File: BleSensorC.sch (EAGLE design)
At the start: 20 parts, among them IC1 PIC16LF18446-I_SS, IC2 SI7020-A20-GM, Q1 SI2333DDS-T1-GE3, T1 VEMT2523SLX01, U1 RN4871-I

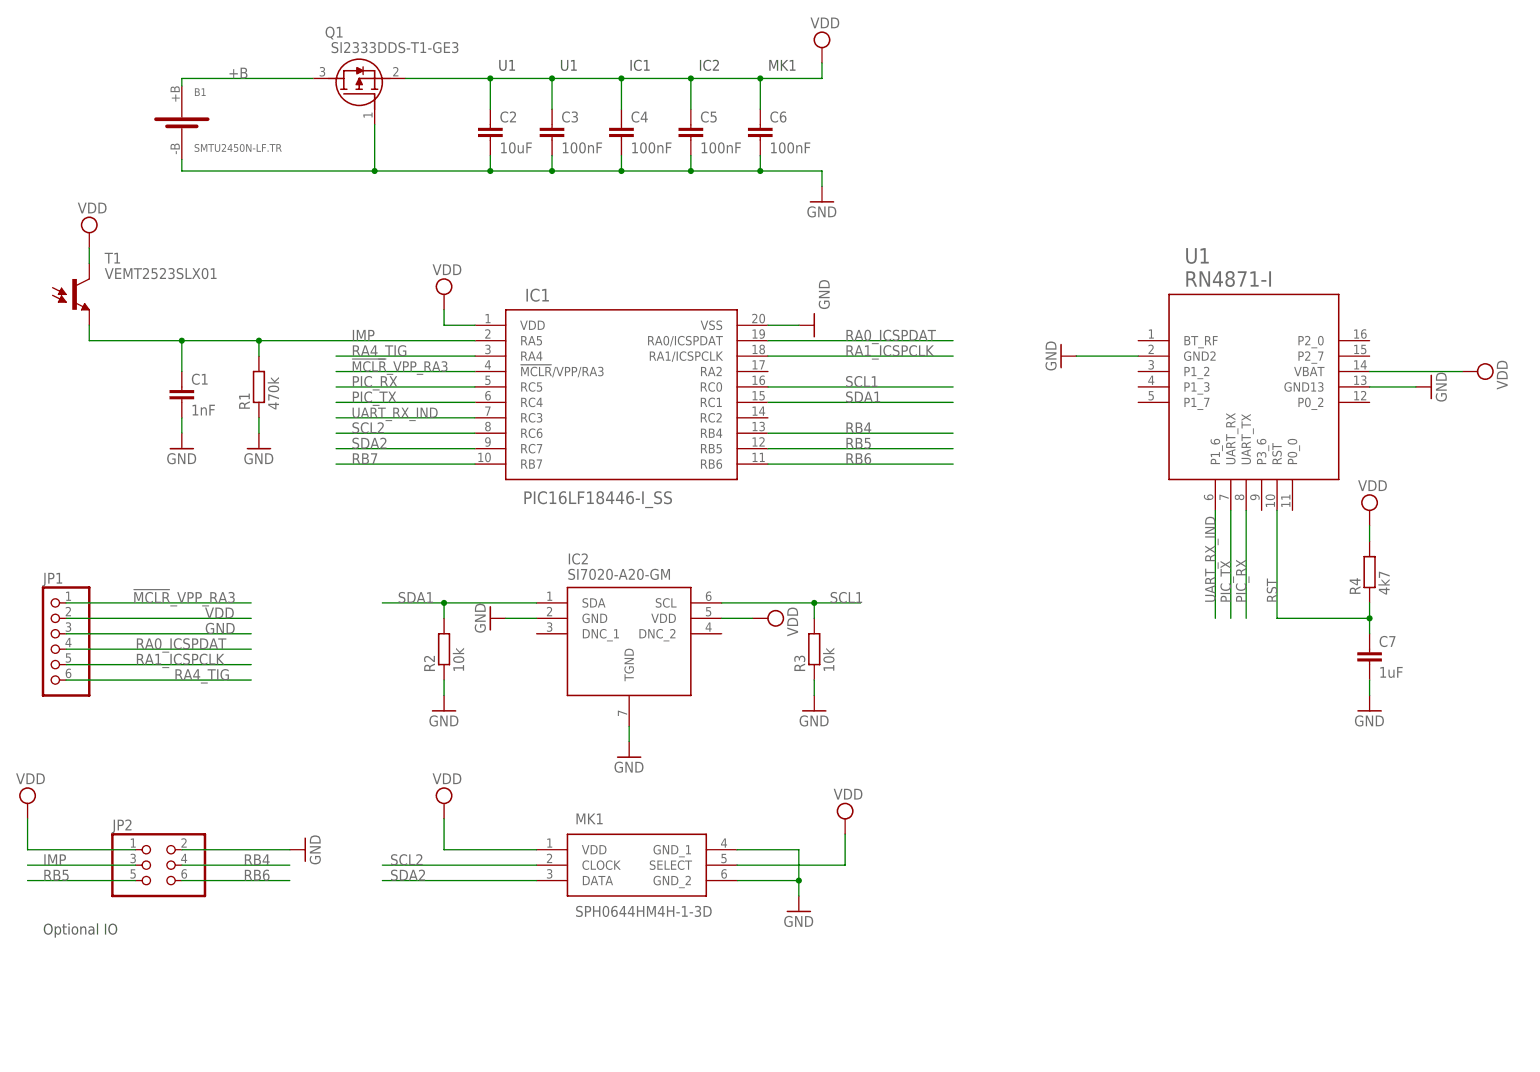
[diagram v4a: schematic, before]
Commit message: IC1 to bottom side
IC1 to bottom side
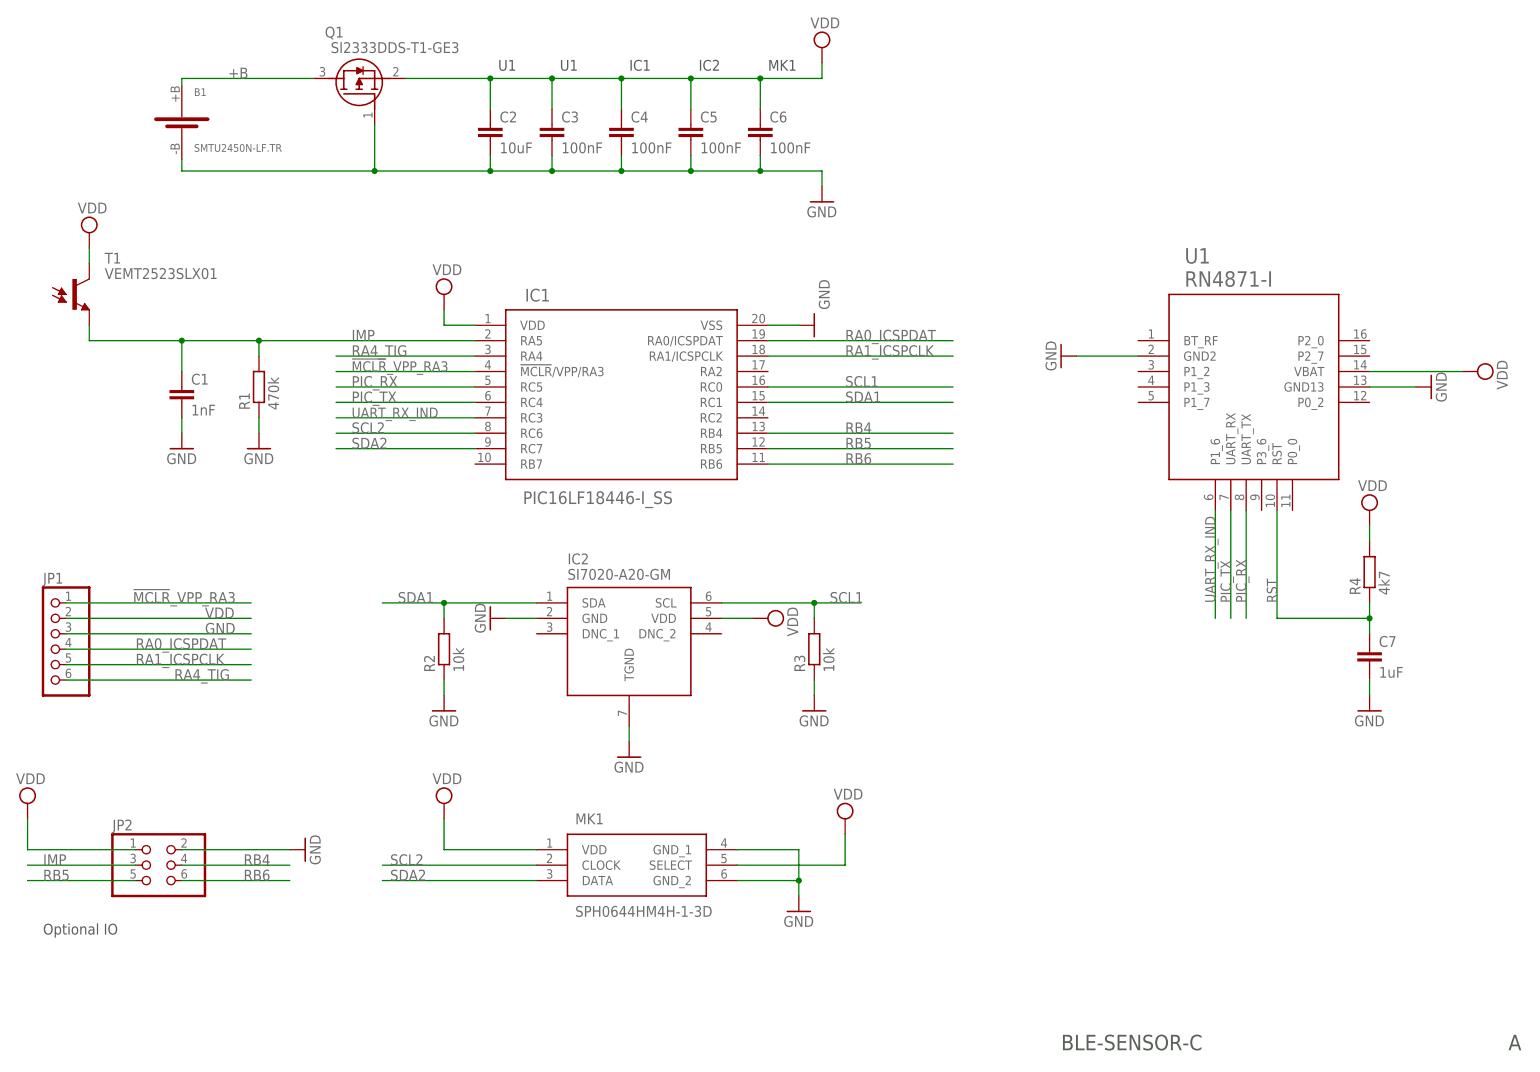
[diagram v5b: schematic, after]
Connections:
- removed net RB7: IC1.RB7
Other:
- note added: "A"
- note added: "BLE-SENSOR-C"
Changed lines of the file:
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@@
 </classes>
 <parts>
-<part name="FRAME1" library="frames" library_urn="urn:adsk.eagle:library:229" deviceset="DINA4_L" device=""/>
+<part name="FRAME1" library="frames" library_urn="urn:adsk.eagle:library:229" deviceset="DINA4_L" device="" value="BLE-SENSOR-C">
+<attribute name="SPICEPREFIX" value="X"/>
+</part>
 <part name="C2" library="resistor" library_urn="urn:adsk.eagle:library:348" deviceset="C-EU" device="C0603" package3d_urn="urn:adsk.eagle:package:23616/2" value="10uF"/>
 <part name="C3" library="resistor" library_urn="urn:adsk.eagle:library:348" deviceset="C-EU" device="C0603" package3d_urn="urn:adsk.eagle:package:23616/2" value="100nF"/>
@@
 <text x="132.08" y="168.91" size="1.778" layer="97">MK1</text>
 <text x="12.7" y="26.67" size="1.778" layer="97">Optional IO</text>
+<text x="180.34" y="7.62" size="2.54" layer="97">BLE-SENSOR-C</text>
+<text x="254" y="7.62" size="2.54" layer="97">A</text>
 </plain>
 <instances>
@@
 </segment>
 </net>
-<net name="RB7" class="0">
-<segment>
-<pinref part="IC1" gate="G$1" pin="RB7"/>
-<wire x1="83.82" y1="104.14" x2="60.96" y2="104.14" width="0.1524" layer="91"/>
-<label x="63.5" y="104.14" size="1.778" layer="95"/>
-</segment>
-</net>

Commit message: Fixed layout, BOM & Gerber files
Fixed layout, BOM & Gerber files
ITEAD PCBA Enquiry
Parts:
- added T2: VEMT2523SLX01, esao:VEMT2523SLX01
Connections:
- new net RA2: IC1.RA2, U1.P2_0
- net IMP: now also T2.E
- net VDD: now also T2.C
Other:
- note added: "NOTE! T2 OPTIONAL"
- moved on the sheet: T1
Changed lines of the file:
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@@
 <part name="U1" library="esao" library_urn="urn:adsk.eagle:library:6645685" deviceset="RN4871-I" device="" package3d_urn="urn:adsk.eagle:package:6331360/16"/>
 <part name="T1" library="esao" library_urn="urn:adsk.eagle:library:6645685" deviceset="VEMT2523SLX01" device="" package3d_urn="urn:adsk.eagle:package:6993138/2"/>
+<part name="T2" library="esao" library_urn="urn:adsk.eagle:library:6645685" deviceset="VEMT2523SLX01" device="" package3d_urn="urn:adsk.eagle:package:6993138/2"/>
+<part name="SUPPLY7" library="supply2" library_urn="urn:adsk.eagle:library:372" deviceset="VDD" device=""/>
 </parts>
 <sheets>
@@
 <text x="180.34" y="7.62" size="2.54" layer="97">BLE-SENSOR-C</text>
 <text x="254" y="7.62" size="2.54" layer="97">A</text>
+<text x="53.34" y="142.24" size="1.778" layer="97">NOTE! T2 OPTIONAL </text>
 </plain>
 <instances>
@@
 <attribute name="VALUE" x="142.875" y="48.895" size="1.778" layer="96"/>
 </instance>
-<instance part="SUPPLY2" gate="G$1" x="20.32" y="142.24" smashed="yes">
-<attribute name="VALUE" x="18.415" y="145.415" size="1.778" layer="96"/>
+<instance part="SUPPLY2" gate="G$1" x="17.78" y="142.24" smashed="yes">
+<attribute name="VALUE" x="15.875" y="145.415" size="1.778" layer="96"/>
 </instance>
 <instance part="GND6" gate="1" x="109.22" y="55.88" smashed="yes">
@@
 <attribute name="VALUE" x="200.66" y="135.89" size="2.54" layer="96" align="top-left"/>
 </instance>
-<instance part="T1" gate="G$1" x="17.78" y="132.08" smashed="yes">
-<attribute name="NAME" x="22.86" y="137.16" size="1.778" layer="95"/>
-<attribute name="VALUE" x="22.86" y="134.62" size="1.778" layer="96"/>
+<instance part="T1" gate="G$1" x="15.24" y="132.08" smashed="yes">
+<attribute name="NAME" x="20.32" y="137.16" size="1.778" layer="95"/>
+<attribute name="VALUE" x="20.32" y="134.62" size="1.778" layer="96"/>
+</instance>
+<instance part="T2" gate="G$1" x="45.72" y="132.08" smashed="yes">
+<attribute name="NAME" x="50.8" y="137.16" size="1.778" layer="95"/>
+<attribute name="VALUE" x="50.8" y="134.62" size="1.778" layer="96"/>
+</instance>
+<instance part="SUPPLY7" gate="G$1" x="48.26" y="142.24" smashed="yes">
+<attribute name="VALUE" x="46.355" y="145.415" size="1.778" layer="96"/>
 </instance>
 </instances>
@@
 <segment>
 <pinref part="SUPPLY2" gate="G$1" pin="VDD"/>
-<wire x1="20.32" y1="137.16" x2="20.32" y2="139.7" width="0.1524" layer="91"/>
+<wire x1="17.78" y1="137.16" x2="17.78" y2="139.7" width="0.1524" layer="91"/>
 <pinref part="T1" gate="G$1" pin="C"/>
 </segment>
@@
 <pinref part="SUPPLY1" gate="G$1" pin="VDD"/>
 <wire x1="10.16" y1="45.72" x2="10.16" y2="40.64" width="0.1524" layer="91"/>
+</segment>
+<segment>
+<pinref part="T2" gate="G$1" pin="C"/>
+<pinref part="SUPPLY7" gate="G$1" pin="VDD"/>
+<wire x1="48.26" y1="137.16" x2="48.26" y2="139.7" width="0.1524" layer="91"/>
 </segment>
 </net>
@@
 <label x="63.5" y="124.46" size="1.778" layer="95"/>
 <pinref part="T1" gate="G$1" pin="E"/>
-<wire x1="20.32" y1="127" x2="20.32" y2="124.46" width="0.1524" layer="91"/>
-<wire x1="20.32" y1="124.46" x2="35.56" y2="124.46" width="0.1524" layer="91"/>
+<wire x1="17.78" y1="127" x2="17.78" y2="124.46" width="0.1524" layer="91"/>
+<wire x1="17.78" y1="124.46" x2="35.56" y2="124.46" width="0.1524" layer="91"/>
 <junction x="35.56" y="124.46"/>
+<pinref part="T2" gate="G$1" pin="E"/>
+<wire x1="48.26" y1="124.46" x2="48.26" y2="127" width="0.1524" layer="91"/>
 </segment>
 <segment>
@@
 </segment>
 </net>
+<net name="RA2" class="0">
+<segment>
+<pinref part="IC1" gate="G$1" pin="RA2"/>
+<wire x1="132.08" y1="119.38" x2="162.56" y2="119.38" width="0.1524" layer="91"/>
+<label x="144.78" y="119.38" size="1.778" layer="95"/>
+</segment>
+<segment>
+<pinref part="U1" gate="G$1" pin="P2_0"/>
+<wire x1="231.14" y1="124.46" x2="246.38" y2="124.46" width="0.1524" layer="91"/>
+<label x="238.76" y="124.46" size="1.778" layer="95"/>
+</segment>
+</net>

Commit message: Seeed order v1.00
Footprint R0805 and C0805
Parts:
- C1, C2, C3, C4, C5, C6, C7: device resistor:C-EUC0603 -> resistor:C-EUC0805
- R1, R2, R3, R4: device resistor:R-EU_R0603 -> resistor:R-EU_R0805
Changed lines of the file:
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@@
 <attribute name="SPICEPREFIX" value="X"/>
 </part>
-<part name="C2" library="resistor" library_urn="urn:adsk.eagle:library:348" deviceset="C-EU" device="C0603" package3d_urn="urn:adsk.eagle:package:23616/2" value="10uF"/>
-<part name="C3" library="resistor" library_urn="urn:adsk.eagle:library:348" deviceset="C-EU" device="C0603" package3d_urn="urn:adsk.eagle:package:23616/2" value="100nF"/>
-<part name="C4" library="resistor" library_urn="urn:adsk.eagle:library:348" deviceset="C-EU" device="C0603" package3d_urn="urn:adsk.eagle:package:23616/2" value="100nF"/>
-<part name="C1" library="resistor" library_urn="urn:adsk.eagle:library:348" deviceset="C-EU" device="C0603" package3d_urn="urn:adsk.eagle:package:23616/2" value="1nF"/>
+<part name="C2" library="resistor" library_urn="urn:adsk.eagle:library:348" deviceset="C-EU" device="C0805" package3d_urn="urn:adsk.eagle:package:23617/2" value="10uF"/>
+<part name="C3" library="resistor" library_urn="urn:adsk.eagle:library:348" deviceset="C-EU" device="C0805" package3d_urn="urn:adsk.eagle:package:23617/2" value="100nF"/>
+<part name="C4" library="resistor" library_urn="urn:adsk.eagle:library:348" deviceset="C-EU" device="C0805" package3d_urn="urn:adsk.eagle:package:23617/2" value="100nF"/>
+<part name="C1" library="resistor" library_urn="urn:adsk.eagle:library:348" deviceset="C-EU" device="C0805" package3d_urn="urn:adsk.eagle:package:23617/2" value="1nF"/>
 <part name="GND1" library="supply1" library_urn="urn:adsk.eagle:library:371" deviceset="GND" device=""/>
 <part name="GND10" library="supply1" library_urn="urn:adsk.eagle:library:371" deviceset="GND" device=""/>
 <part name="GND13" library="supply1" library_urn="urn:adsk.eagle:library:371" deviceset="GND" device=""/>
 <part name="GND11" library="supply1" library_urn="urn:adsk.eagle:library:371" deviceset="GND" device=""/>
-<part name="R1" library="resistor" library_urn="urn:adsk.eagle:library:348" deviceset="R-EU_" device="R0603" package3d_urn="urn:adsk.eagle:package:23555/2" value="470k"/>
+<part name="R1" library="resistor" library_urn="urn:adsk.eagle:library:348" deviceset="R-EU_" device="R0805" package3d_urn="urn:adsk.eagle:package:23553/2" value="470k"/>
 <part name="IC2" library="esao" library_urn="urn:adsk.eagle:library:6645685" deviceset="SI7020-A20-GM" device="" package3d_urn="urn:adsk.eagle:package:6645708/4"/>
 <part name="GND5" library="supply1" library_urn="urn:adsk.eagle:library:371" deviceset="GND" device=""/>
-<part name="C5" library="resistor" library_urn="urn:adsk.eagle:library:348" deviceset="C-EU" device="C0603" package3d_urn="urn:adsk.eagle:package:23616/2" value="100nF"/>
-<part name="R2" library="resistor" library_urn="urn:adsk.eagle:library:348" deviceset="R-EU_" device="R0603" package3d_urn="urn:adsk.eagle:package:23555/2" value="10k"/>
-<part name="R3" library="resistor" library_urn="urn:adsk.eagle:library:348" deviceset="R-EU_" device="R0603" package3d_urn="urn:adsk.eagle:package:23555/2" value="10k"/>
+<part name="C5" library="resistor" library_urn="urn:adsk.eagle:library:348" deviceset="C-EU" device="C0805" package3d_urn="urn:adsk.eagle:package:23617/2" value="100nF"/>
+<part name="R2" library="resistor" library_urn="urn:adsk.eagle:library:348" deviceset="R-EU_" device="R0805" package3d_urn="urn:adsk.eagle:package:23553/2" value="10k"/>
+<part name="R3" library="resistor" library_urn="urn:adsk.eagle:library:348" deviceset="R-EU_" device="R0805" package3d_urn="urn:adsk.eagle:package:23553/2" value="10k"/>
 <part name="GND2" library="supply1" library_urn="urn:adsk.eagle:library:371" deviceset="GND" device=""/>
 <part name="GND4" library="supply1" library_urn="urn:adsk.eagle:library:371" deviceset="GND" device=""/>
@@
 <part name="GND7" library="supply1" library_urn="urn:adsk.eagle:library:371" deviceset="GND" device=""/>
 <part name="$1_40_$_2018-11-18_09-41-28" library="supply2" library_urn="urn:adsk.eagle:library:372" deviceset="VDD" device=""/>
-<part name="R4" library="resistor" library_urn="urn:adsk.eagle:library:348" deviceset="R-EU_" device="R0603" package3d_urn="urn:adsk.eagle:package:23555/2" value="4k7"/>
-<part name="C7" library="resistor" library_urn="urn:adsk.eagle:library:348" deviceset="C-EU" device="C0603" package3d_urn="urn:adsk.eagle:package:23616/2" value="1uF"/>
+<part name="R4" library="resistor" library_urn="urn:adsk.eagle:library:348" deviceset="R-EU_" device="R0805" package3d_urn="urn:adsk.eagle:package:23553/2" value="4k7"/>
+<part name="C7" library="resistor" library_urn="urn:adsk.eagle:library:348" deviceset="C-EU" device="C0805" package3d_urn="urn:adsk.eagle:package:23617/2" value="1uF"/>
 <part name="GND12" library="supply1" library_urn="urn:adsk.eagle:library:371" deviceset="GND" device=""/>
 <part name="$1_39_$_2018-11-18_09-41-28" library="supply2" library_urn="urn:adsk.eagle:library:372" deviceset="VDD" device=""/>
-<part name="C6" library="resistor" library_urn="urn:adsk.eagle:library:348" deviceset="C-EU" device="C0603" package3d_urn="urn:adsk.eagle:package:23616/2" value="100nF"/>
+<part name="C6" library="resistor" library_urn="urn:adsk.eagle:library:348" deviceset="C-EU" device="C0805" package3d_urn="urn:adsk.eagle:package:23617/2" value="100nF"/>
 <part name="$1_38_$_2018-11-18_09-41-28" library="supply2" library_urn="urn:adsk.eagle:library:372" deviceset="VDD" device=""/>
 <part name="SUPPLY2" library="supply2" library_urn="urn:adsk.eagle:library:372" deviceset="VDD" device=""/>
